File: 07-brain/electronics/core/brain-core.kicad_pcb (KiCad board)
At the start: 2 copper layers, 58 x 110 mm, 96 parts, among them J1 Conn_02x03_Odd_Even, J10 Conn_01x02, J2 Conn_02x02_Odd_Even, J3 Conn_02x02_Odd_Even, J4 Conn_02x03_Odd_Even, J5 Conn_01x02, J6 Conn_02x05_Odd_Even, J7 Conn_02x05_Odd_Even, J8 Conn_02x03_Odd_Even, J9 Conn_01x02, Q1 MMBT3904, Q3 MMBT3904, Q6 MMBT3904, Q7 MMBT3904, SW1 SW_SPST, U1 LM7805_TO220, U10 74HC4051, U2 6N137, U3 Pico, U4 TL072, U5 TL072, U6 MCP4822, U7 74HC4053B, U8 TL072, U9 TL072

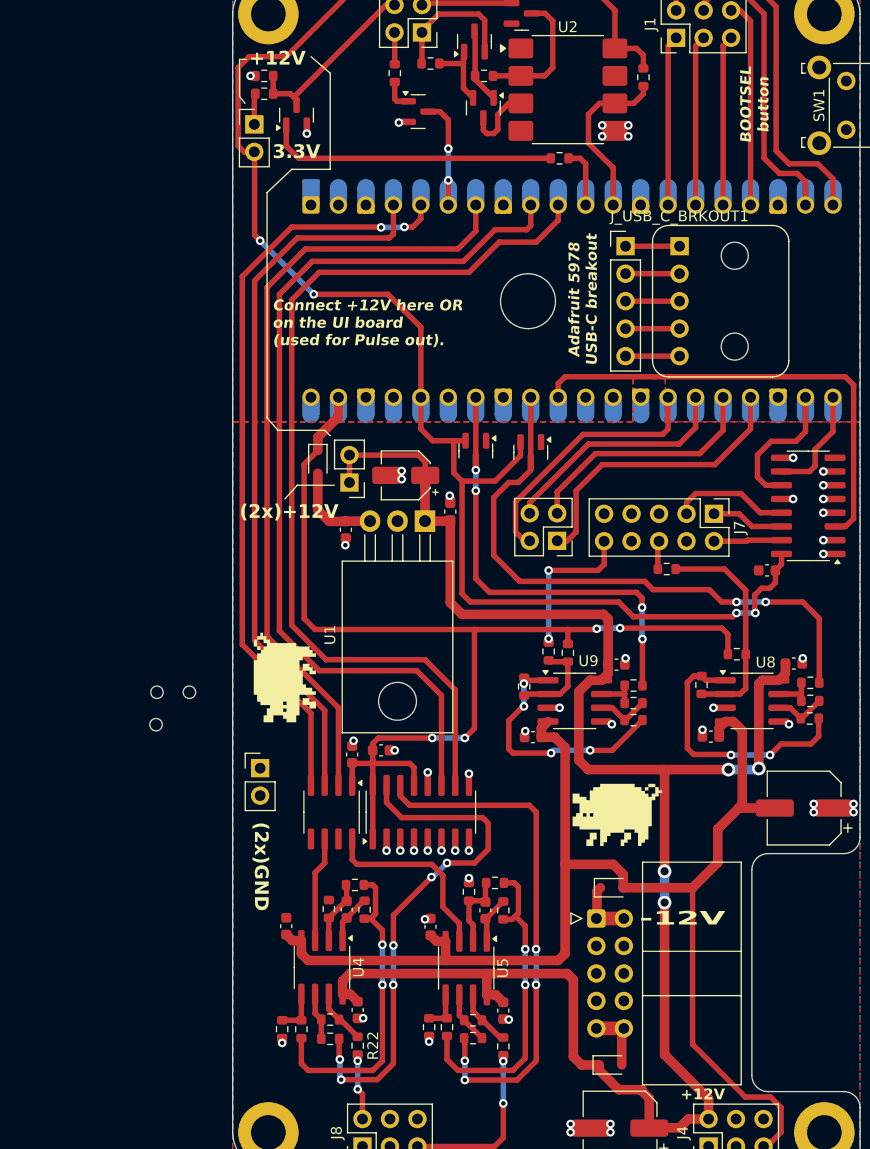
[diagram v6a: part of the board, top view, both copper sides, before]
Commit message: Started via stitching on Brain Core
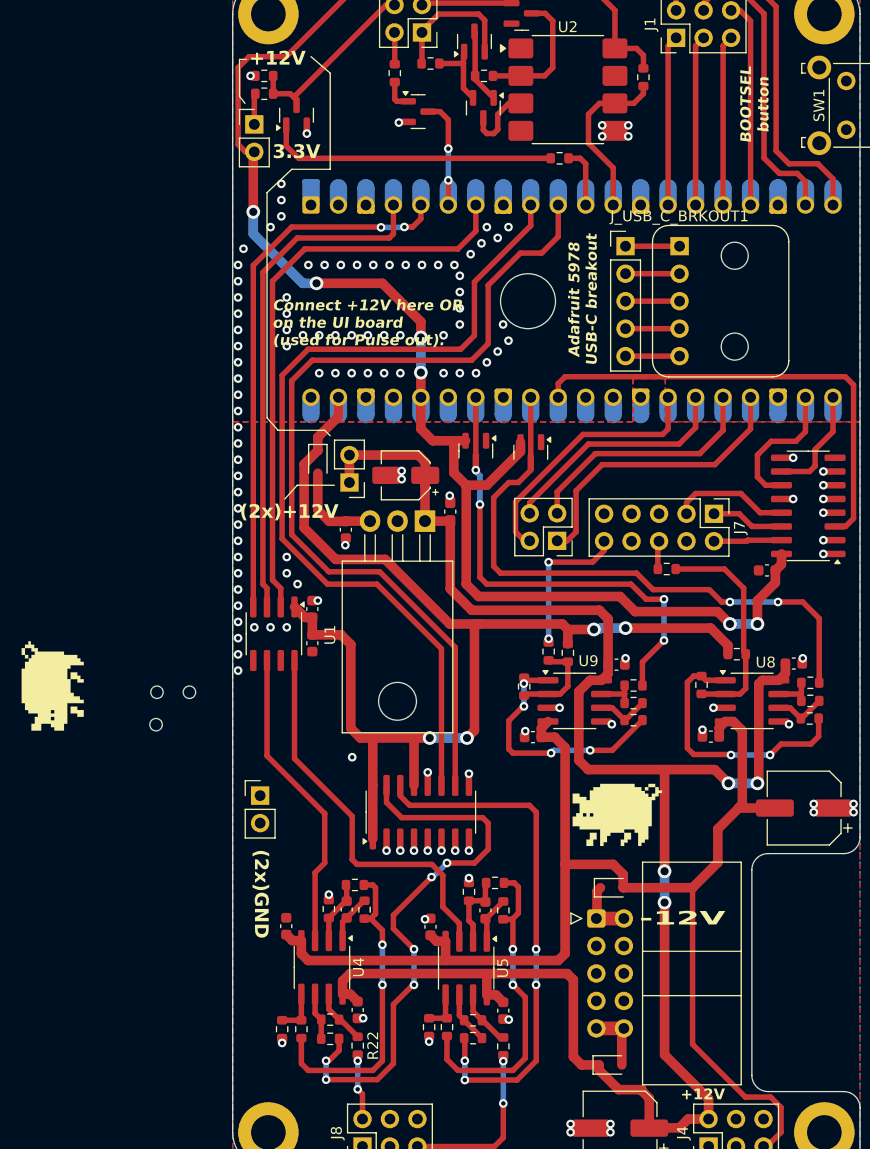
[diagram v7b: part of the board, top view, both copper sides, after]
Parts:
- moved G*** 21.5 mm to (107.4, 109.4)
- moved U6 17.3 mm to (127.8, 104.6)
- moved C17 13.9 mm to (131.4, 102.3)
- moved C18 11.8 mm to (131.4, 105.5), turned to -90 degrees
- moved J5 2.54 mm to (126.5, 119.6)
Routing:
- net /GPIO_3: track 69.7 -> 50.2 mm
- net /GPIO_2: track 66.6 -> 47.3 mm
- net /GPIO_5: track 72.6 -> 53.6 mm
- net Net-(U5A-+): track 17.6 -> 36.3 mm
- net Net-(U4A-+): track 9.77 -> 28.5 mm
- net +5V: track 102.4 -> 110.3 mm
- net /GPIO_6: track 84.7 -> 80.2 mm
- net Net-(U7-B): track 48.5 -> 52.1 mm
- net /GPIO_7: track 85.6 -> 82.7 mm
- net /GPIO_28: track 40.1 -> 42.6 mm
- net +12V: track 173.9 -> 175.0 mm
- net +3.3V: track 153.9 -> 153.2 mm, vias 4 -> 6
- net /GPIO_27: track 55.0 -> 55.6 mm
- net GND: vias 52 -> 134

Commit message: More stitching on Brain
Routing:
- net GND: vias 134 -> 280
